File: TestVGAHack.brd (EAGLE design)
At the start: 70.1 x 24 mm, 0 parts

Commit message: Updated VGA hack board
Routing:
- net C1: track 0.00 -> 102.9 mm, vias 2 -> 3
- net C11: track 0.00 -> 102.6 mm, vias 2 -> 3
- net C2_11: track 0.00 -> 102.0 mm, vias 2 -> 3
- net C2_1: track 0.00 -> 101.7 mm, vias 2 -> 3
- net C2: track 0.00 -> 90.8 mm, vias 2 -> 3
- net C12: track 0.00 -> 90.5 mm, vias 2 -> 3
- net C2_12: track 0.00 -> 90.0 mm, vias 2 -> 3
- net C2_2: track 0.00 -> 89.6 mm, vias 2 -> 3
- net C3: track 0.00 -> 78.7 mm, vias 2 -> 3
- net C13: track 0.00 -> 78.4 mm, vias 2 -> 3
- net C2_13: track 0.00 -> 77.9 mm, vias 2 -> 3
- net C2_3: track 0.00 -> 77.5 mm, vias 2 -> 3
- net C4: track 0.00 -> 66.5 mm, vias 2 -> 3
- net C14: track 0.00 -> 66.2 mm, vias 2 -> 3
- net C2_14: track 0.00 -> 65.7 mm, vias 2 -> 3
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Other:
- board size 70.1 x 24 mm -> 83.6 x 49.2 mm

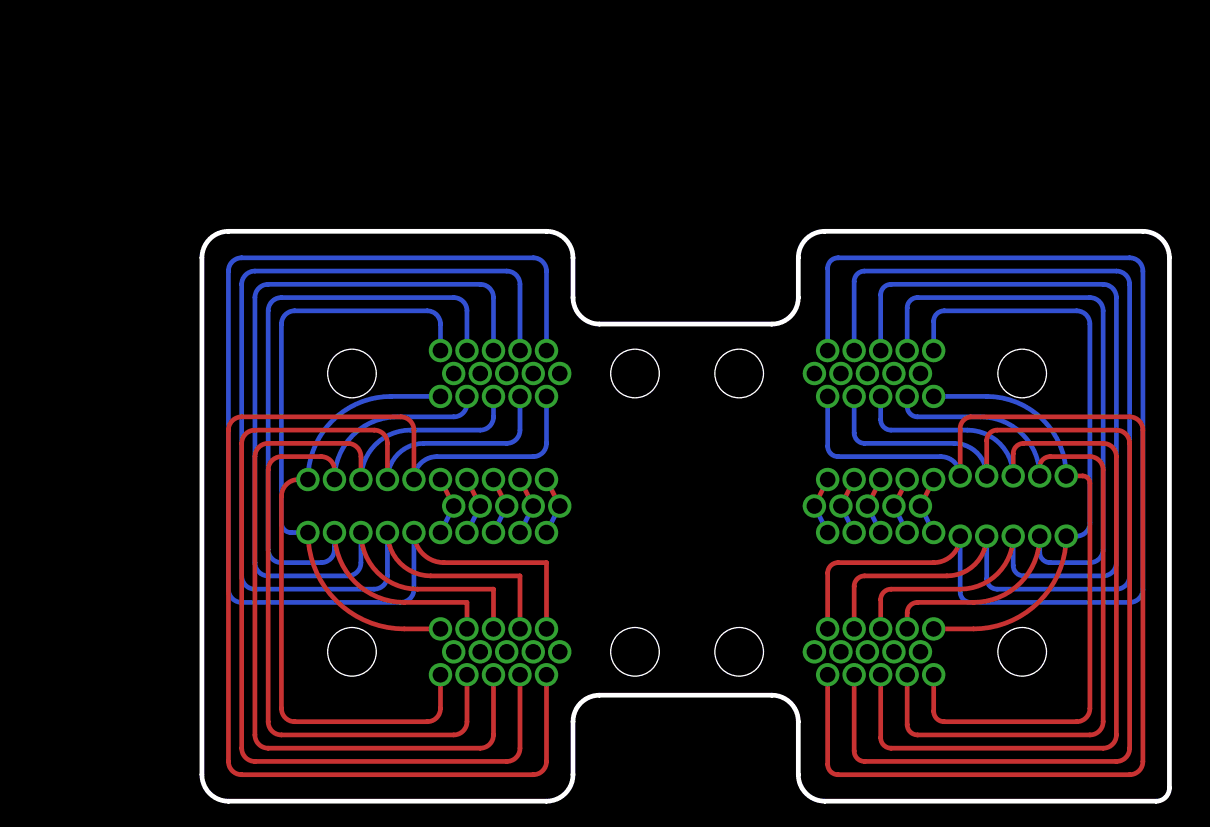
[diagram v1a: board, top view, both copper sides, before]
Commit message: Updated VGA hcak board more Should now have spots for I2C and UART connections
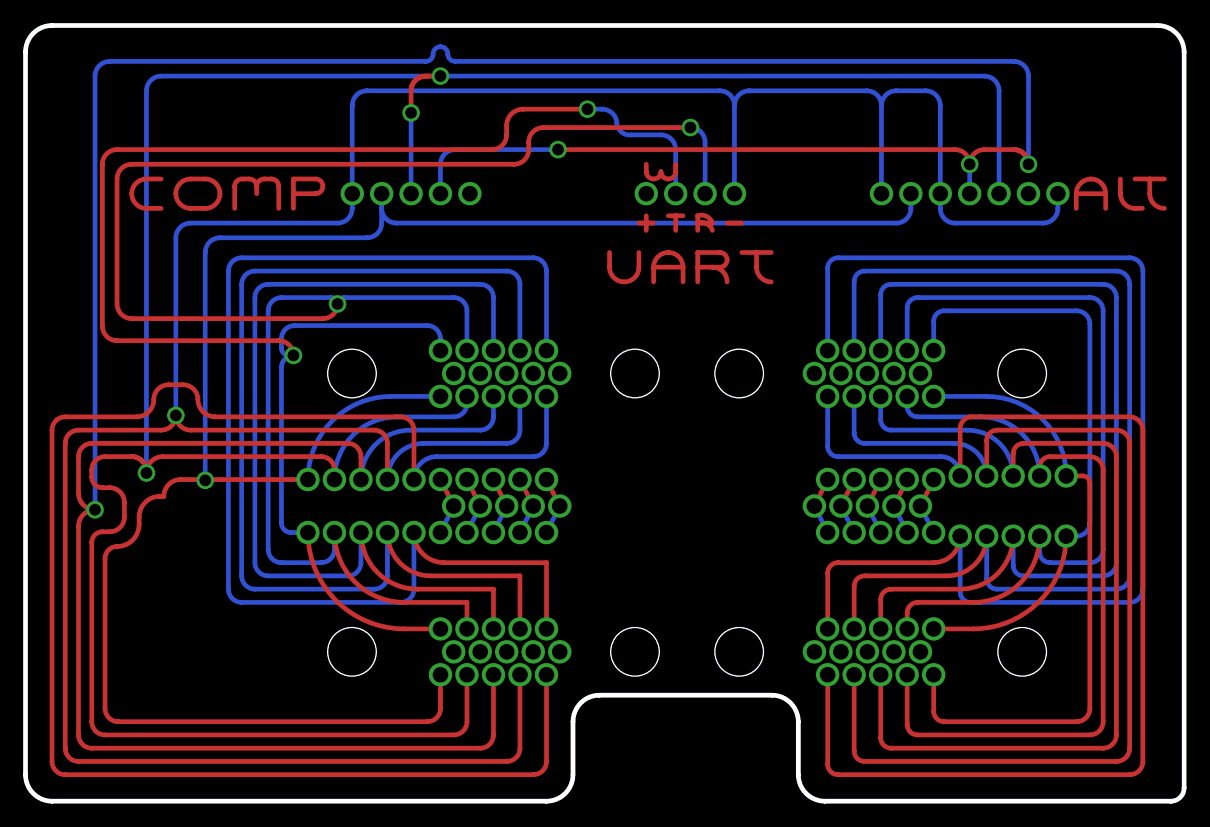
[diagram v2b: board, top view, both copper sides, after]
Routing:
- net C13: track 78.4 -> 297.6 mm, vias 3 -> 9
- net C14: track 66.2 -> 233.2 mm, vias 3 -> 8
- net C12: track 90.5 -> 253.1 mm, vias 3 -> 9
- net C15: track 53.2 -> 167.6 mm, vias 3 -> 6
- net C4: track 66.5 -> 155.9 mm, vias 3 -> 6
- net C5: track 51.7 -> 138.9 mm, vias 3 -> 6
- net C11: track 102.6 -> 135.4 mm
- net S$9: track 0.00 -> 9.94 mm
- net S$13: track 0.00 -> 9.72 mm
- net S$14: track 0.00 -> 9.31 mm
- net S$4: track 0.00 -> 8.67 mm
- net S$1: track 0.00 -> 8.67 mm
- net S$15: track 0.00 -> 8.15 mm
- net S$7: track 0.00 -> 6.13 mm
- net S$12: track 0.00 -> 6.13 mm
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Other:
- board size 83.6 x 49.2 mm -> 100.1 x 67 mm

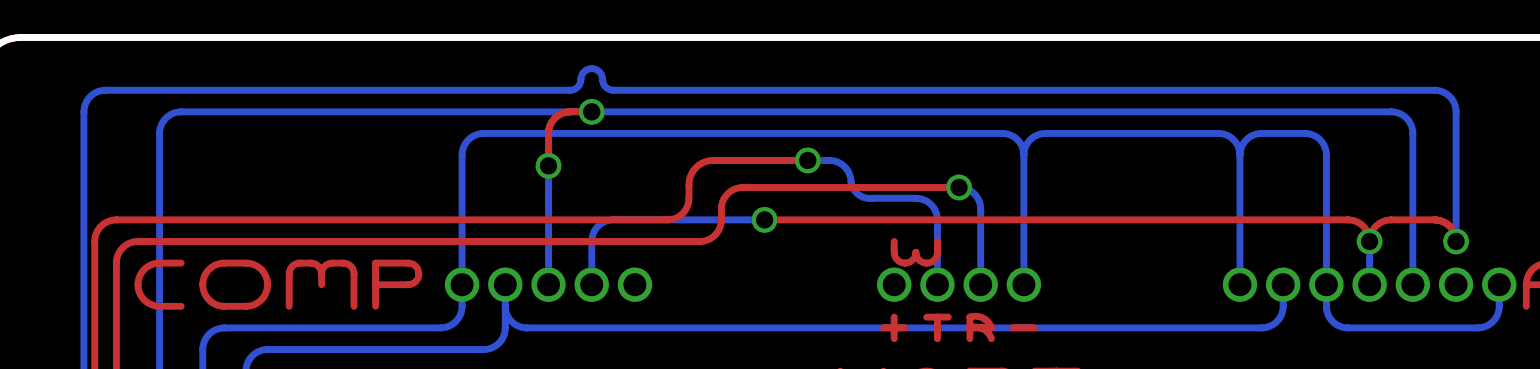
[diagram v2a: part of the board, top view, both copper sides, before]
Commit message: Various changes to the board. With this, the testing setup has been functional for quite a while...
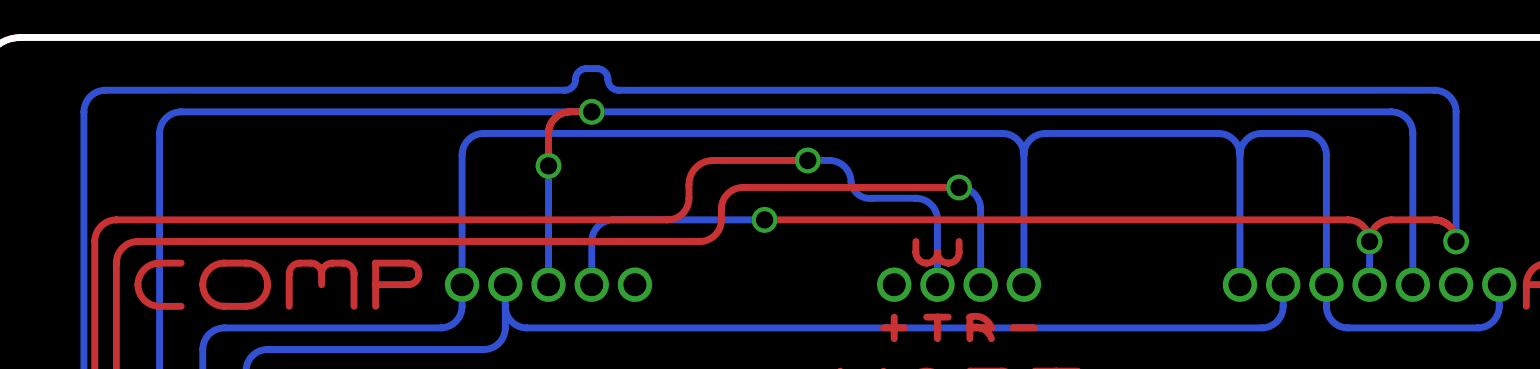
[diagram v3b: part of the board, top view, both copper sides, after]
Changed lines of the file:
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@@
 <wire x1="49.53" y1="36.83" x2="50.8" y2="35.56" width="0.4064" layer="1" curve="-90"/>
 <via x="50.8" y="35.56" extent="1-16" drill="1.016" shape="octagon"/>
-<wire x1="49.53" y1="44.45" x2="1.27" y2="44.45" width="0.4064" layer="16"/>
-<wire x1="1.27" y1="44.45" x2="0.635" y2="45.085" width="0.4064" layer="16" curve="-90"/>
-<wire x1="0.635" y1="45.085" x2="0" y2="45.72" width="0.4064" layer="16" curve="90"/>
-<wire x1="0" y1="45.72" x2="-0.635" y2="45.085" width="0.4064" layer="16" curve="90"/>
-<wire x1="-0.635" y1="45.085" x2="-1.27" y2="44.45" width="0.4064" layer="16" curve="-90"/>
-<wire x1="-1.27" y1="44.45" x2="-28.575" y2="44.45" width="0.4064" layer="16"/>
+<wire x1="49.53" y1="44.45" x2="1.5875" y2="44.45" width="0.4064" layer="16"/>
+<wire x1="1.5875" y1="44.45" x2="0.9525" y2="45.085" width="0.4064" layer="16" curve="-90"/>
+<wire x1="-0.9525" y1="45.085" x2="-1.5875" y2="44.45" width="0.4064" layer="16" curve="-90"/>
+<wire x1="-1.5875" y1="44.45" x2="-28.575" y2="44.45" width="0.4064" layer="16"/>
 <wire x1="-28.575" y1="44.45" x2="-29.845" y2="43.18" width="0.4064" layer="16" curve="90"/>
 <wire x1="-29.845" y1="43.18" x2="-29.845" y2="5.715" width="0.4064" layer="16"/>
@@
 <wire x1="50.8" y1="35.56" x2="50.8" y2="43.18" width="0.4064" layer="16"/>
 <wire x1="50.8" y1="43.18" x2="49.53" y2="44.45" width="0.4064" layer="16" curve="90"/>
+<wire x1="-0.3175" y1="45.72" x2="-0.9525" y2="45.085" width="0.4064" layer="16" curve="90"/>
+<wire x1="0.9525" y1="45.085" x2="0.3175" y2="45.72" width="0.4064" layer="16" curve="90"/>
+<wire x1="-0.3175" y1="45.72" x2="0.3175" y2="45.72" width="0.4064" layer="16"/>
 </signal>
 <signal name="C12">
@@
 </signal>
 <signal name="S$16">
-<wire x1="17.78" y1="35.56" x2="17.78" y2="34.925" width="0.4064" layer="1"/>
-<wire x1="17.78" y1="34.925" x2="18.415" y2="34.29" width="0.4064" layer="1" curve="90"/>
-<wire x1="18.415" y1="34.29" x2="19.05" y2="34.925" width="0.4064" layer="1" curve="90"/>
+<wire x1="19.05" y1="35.56" x2="19.05" y2="34.925" width="0.4064" layer="1"/>
 <wire x1="19.05" y1="34.925" x2="19.685" y2="34.29" width="0.4064" layer="1" curve="90"/>
 <wire x1="19.685" y1="34.29" x2="20.32" y2="34.925" width="0.4064" layer="1" curve="90"/>
-<wire x1="20.32" y1="34.925" x2="20.32" y2="35.56" width="0.4064" layer="1"/>
+<wire x1="20.32" y1="34.925" x2="20.955" y2="34.29" width="0.4064" layer="1" curve="90"/>
+<wire x1="20.955" y1="34.29" x2="21.59" y2="34.925" width="0.4064" layer="1" curve="90"/>
+<wire x1="21.59" y1="34.925" x2="21.59" y2="35.56" width="0.4064" layer="1"/>
 </signal>
 </signals>
